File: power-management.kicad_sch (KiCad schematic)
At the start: 18 parts, among them Q3 DMP2070UQ-7, U2 AP2112K-3.3, U6 AP3602AKTR-G1

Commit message: Working on layout
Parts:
- Q3: footprint Package_TO_SOT_SMD:SOT-23-5_HandSoldering -> Package_TO_SOT_SMD:TSOT-23
- R38: footprint (none) -> Resistor_SMD:R_0805_2012Metric; Mfr (none) -> YAGEO; Mfr P/N (none) -> RC0805FR-07100KL; Supplier_1 (none) -> Digikey; Supplier_1 P/N (none) -> 311-100KCRCT-ND; Supplier_1 Price @ Qty (none) -> $0.00714; Supplier_1 Unit Price (none) -> $0.10000
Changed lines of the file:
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@@
 			)
 		)
-		(property "Footprint" "Package_TO_SOT_SMD:SOT-23-5_HandSoldering"
+		(property "Footprint" "Package_TO_SOT_SMD:TSOT-23"
 			(at 67.31 91.44 0)
 			(effects
@@
 					(size 1.27 1.27)
 				)
-				(hide yes)
 			)
 		)
@@
 			)
 		)
-		(property "Footprint" ""
+		(property "Footprint" "Resistor_SMD:R_0805_2012Metric"
 			(at 236.22 105.918 90)
 			(effects
@@
 			)
 		)
-		(property "Datasheet" "~"
+		(property "Datasheet" "https://www.yageo.com/upload/media/product/products/datasheet/rchip/PYu-RC_Group_51_RoHS_L_12.pdf"
 			(at 236.22 104.14 0)
 			(effects
@@
 			)
 		)
-		(property "Mfr" ""
-			(at 236.22 104.14 0)
-			(effects
-				(font
-					(size 1.27 1.27)
-				)
-				(hide yes)
-			)
-		)
-		(property "Mfr P/N" ""
-			(at 236.22 104.14 0)
-			(effects
-				(font
-					(size 1.27 1.27)
-				)
-				(hide yes)
-			)
-		)
-		(property "Supplier_1" ""
-			(at 236.22 104.14 0)
-			(effects
-				(font
-					(size 1.27 1.27)
-				)
-				(hide yes)
-			)
-		)
-		(property "Supplier_1 P/N" ""
-			(at 236.22 104.14 0)
-			(effects
-				(font
-					(size 1.27 1.27)
-				)
-				(hide yes)
-			)
-		)
-		(property "Supplier_1 Unit Price" ""
-			(at 236.22 104.14 0)
-			(effects
-				(font
-					(size 1.27 1.27)
-				)
-				(hide yes)
-			)
-		)
-		(property "Supplier_1 Price @ Qty" ""
-			(at 236.22 104.14 0)
-			(effects
+		(property "Mfr" "YAGEO"
+			(at 236.22 104.14 0)
+			(effects
+				(font
+					(size 1.27 1.27)
+				)
+				(hide yes)
+			)
+		)
+		(property "Mfr P/N" "RC0805FR-07100KL"
+			(at 236.22 104.14 0)
+			(effects
+				(font
+					(size 1.27 1.27)
+				)
+				(hide yes)
+			)
+		)
+		(property "Supplier_1" "Digikey"
+			(at 236.22 104.14 0)
+			(effects
+				(font
+					(size 1.27 1.27)
+				)
+				(hide yes)
+			)
+		)
+		(property "Supplier_1 P/N" "311-100KCRCT-ND"
+			(at 236.22 104.14 0)
+			(effects
+				(font
+					(size 1.27 1.27)
+				)
+				(hide yes)
+			)
+		)
+		(property "Supplier_1 Unit Price" "$0.10000 "
+			(at 236.22 104.14 0)
+			(effects
+				(font
+					(size 1.27 1.27)
+				)
+				(hide yes)
+			)
+		)
+		(property "Supplier_1 Price @ Qty" "$0.00714 "
+			(at 236.22 104.14 0)
+			(effects

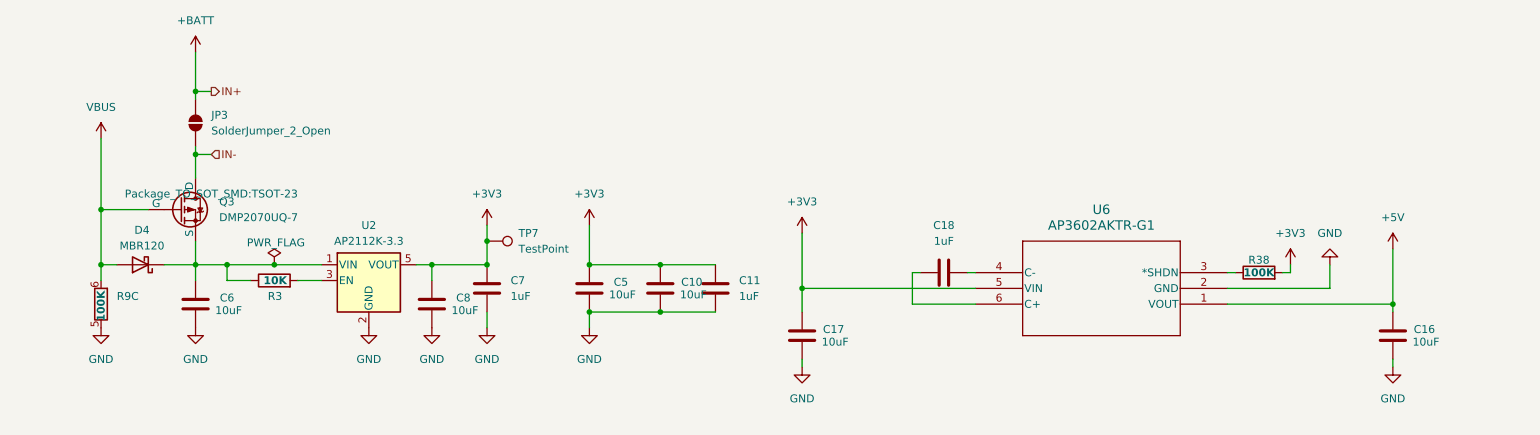
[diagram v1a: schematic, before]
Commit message: Redid board layout. Still have to add bypass caps
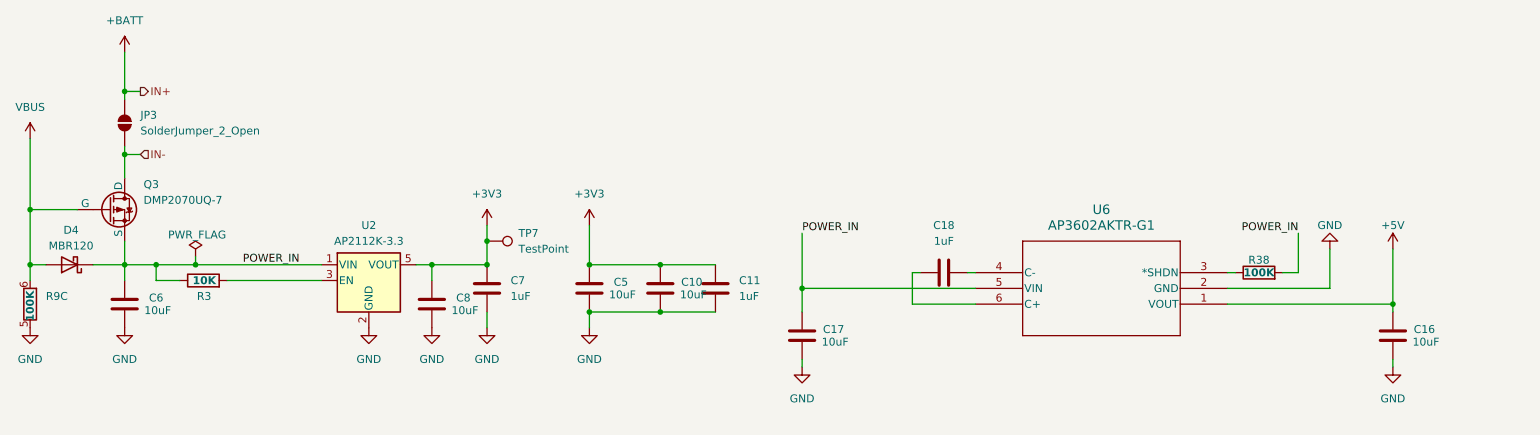
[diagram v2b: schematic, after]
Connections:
- net +3V3: no longer C17.1, R38.2, U6.5 (VIN)
- net POWER_IN: now reaches C6.1, D4.1 (K), Q3.3 (S), R3.1, U2.1 (VIN)
- net POWER_IN: now also C17.1, R38.2, U6.5 (VIN)
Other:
- moved on the sheet: C6, D4, JP3, Q3, R3, R9C

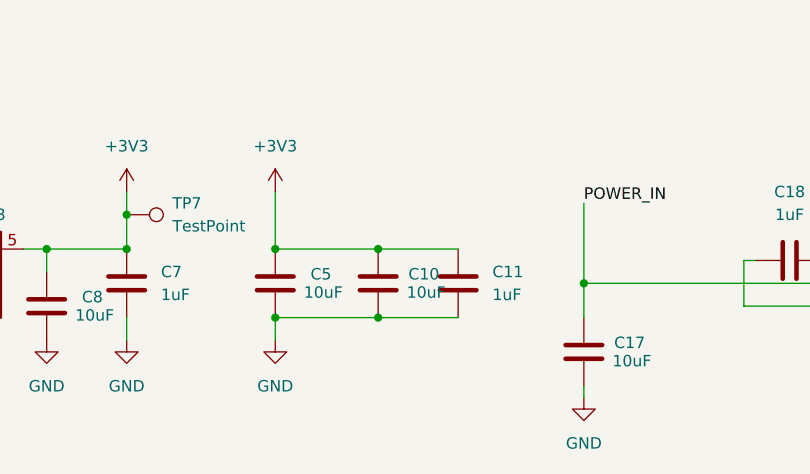
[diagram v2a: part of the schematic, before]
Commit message: Added mounting holes
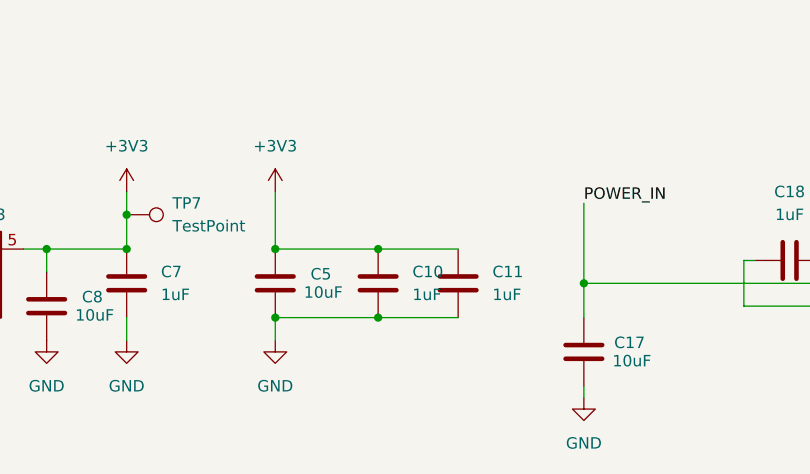
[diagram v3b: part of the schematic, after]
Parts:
- C10: value 10uF -> 1uF; footprint Inductor_SMD:L_0805_2012Metric -> Capacitor_SMD:C_0603_1608Metric; Mfr Samsung Electro-Mechanics -> YAGEO; Mfr P/N CL21A106KOQNNNE -> CC0603KRX7R7BB105; Supplier_1 P/N 1276-1096-1-ND -> 0.10; Supplier_1 Price @ Qty 0.03130 -> (none); Supplier_1 Unit Price 0.10 -> 0.03080
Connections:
- net +3V3: now also C10.2; no longer C10.1
- net GND: now also C10.1; no longer C10.2
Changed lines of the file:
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@@
 	)
 	(junction
-		(at 53.34 74.93)
+		(at 139.7 102.87)
 		(diameter 0)
 		(color 0 0 0 0)
 	)
 	(junction
-		(at 102.87 102.87)
+		(at 53.34 74.93)
 		(diameter 0)
 		(color 0 0 0 0)
 	)
 	(junction
-		(at 139.7 102.87)
+		(at 102.87 102.87)
 		(diameter 0)
 		(color 0 0 0 0)
@@
 	)
 	(junction
-		(at 111.76 102.87)
+		(at 139.7 110.49)
 		(diameter 0)
 		(color 0 0 0 0)
 	)
 	(junction
-		(at 139.7 110.49)
+		(at 111.76 102.87)
 		(diameter 0)
 		(color 0 0 0 0)
@@
 	(wire
 		(pts
+			(xy 139.7 102.87) (xy 148.59 102.87)
+		)
+		(stroke
+			(width 0)
+			(type default)
+		)
+	)
+	(wire
+		(pts
 			(xy 48.26 102.87) (xy 53.34 102.87)
 		)
@@
 	(wire
 		(pts
-			(xy 242.57 97.79) (xy 242.57 104.14)
+			(xy 139.7 110.49) (xy 148.59 110.49)
 		)
 		(stroke
@@
 	(wire
 		(pts
-			(xy 38.1 93.98) (xy 38.1 102.87)
+			(xy 242.57 97.79) (xy 242.57 104.14)
 		)
 		(stroke
@@
 	(wire
 		(pts
-			(xy 64.77 102.87) (xy 85.09 102.87)
+			(xy 38.1 93.98) (xy 38.1 102.87)
 		)
 		(stroke
@@
 	(wire
 		(pts
-			(xy 55.88 74.93) (xy 53.34 74.93)
+			(xy 64.77 102.87) (xy 85.09 102.87)
 		)
 		(stroke
@@
 	(wire
 		(pts
-			(xy 128.27 96.52) (xy 128.27 102.87)
+			(xy 55.88 74.93) (xy 53.34 74.93)
 		)
 		(stroke
@@
 	(wire
 		(pts
-			(xy 128.27 110.49) (xy 128.27 113.03)
+			(xy 128.27 96.52) (xy 128.27 102.87)
 		)
 		(stroke
@@
 	(wire
 		(pts
-			(xy 111.76 99.06) (xy 111.76 102.87)
+			(xy 128.27 110.49) (xy 128.27 113.03)
 		)
 		(stroke
@@
 	(wire
 		(pts
-			(xy 232.41 104.14) (xy 231.14 104.14)
+			(xy 111.76 99.06) (xy 111.76 102.87)
 		)
 		(stroke
@@
 	(wire
 		(pts
-			(xy 128.27 102.87) (xy 139.7 102.87)
+			(xy 232.41 104.14) (xy 231.14 104.14)
 		)
 		(stroke
@@
 	(wire
 		(pts
-			(xy 139.7 102.87) (xy 148.59 102.87)
+			(xy 128.27 102.87) (xy 139.7 102.87)
 		)
 		(stroke
@@
 	(wire
 		(pts
-			(xy 139.7 110.49) (xy 148.59 110.49)
-		)
-		(stroke
-			(width 0)
-			(type default)
-		)
-	)
-	(wire
-		(pts
 			(xy 128.27 110.49) (xy 139.7 110.49)
 		)
@@
 	)
 	(symbol
+		(lib_id "Device:C")
+		(at 139.7 106.68 180)
+		(unit 1)
+		(exclude_from_sim no)
+		(in_bom yes)
+		(on_board yes)
+		(dnp no)
+		(fields_autoplaced yes)
+		(property "Reference" "C10"
+			(at 143.51 105.4099 0)
+			(effects
+				(font
+					(size 1.27 1.27)
+				)
+				(justify right)
+			)
+		)
+		(property "Value" "1uF"
+			(at 143.51 107.9499 0)
+			(effects
+				(font
+					(size 1.27 1.27)
+				)
+				(justify right)
+			)
+		)
+		(property "Footprint" "Capacitor_SMD:C_0603_1608Metric"
+			(at 138.7348 102.87 0)
+			(effects
+				(font
+					(size 1.27 1.27)
+				)
+				(hide yes)
+			)
+		)
+		(property "Datasheet" "https://www.yageo.com/upload/media/product/productsearch/datasheet/mlcc/UPY-GPHC_X7R_6"
+			(at 139.7 106.68 0)
+			(effects
+				(font
+					(size 1.27 1.27)
+					(italic yes)
+				)
+				(hide yes)
+			)
+		)
+		(property "Description" "1 uF 10% 16V Ceramic Capacitor X7R 0603 (1608 Metric)"
+			(at 139.7 106.68 0)
+			(effects
+				(font
+					(size 1.27 1.27)
+				)
+				(hide yes)
+			)
+		)
+		(property "Mfr" "YAGEO"
+			(at 139.7 106.68 0)
+			(effects
+				(font
+					(size 1.27 1.27)
+				)
+				(hide yes)
+			)
+		)
+		(property "Mfr P/N" "CC0603KRX7R7BB105"
+			(at 139.7 106.68 0)
+			(effects
+				(font
+					(size 1.27 1.27)
+					(thickness 0.1588)
+				)
+				(hide yes)
+			)
+		)
+		(property "Supplier_1" "Digikey"
+			(at 139.7 106.68 0)
+			(effects
+				(font
+					(size 1.27 1.27)
+				)
+				(hide yes)
+			)
+		)
+		(property "Supplier_1 P/N" "0.10"
+			(at 139.7 106.68 0)
+			(effects
+				(font
+					(size 1.27 1.27)
+				)
+				(hide yes)
+			)
+		)
+		(property "Supplier_1 Unit Price" "0.03080"
+			(at 139.7 106.68 0)
+			(effects
+				(font
+					(size 1.27 1.27)
+				)
+				(hide yes)
+			)
+		)
+		(property "Supplier_1 Price @ Qty" ""
+			(at 139.7 106.68 0)
+			(effects
+				(font
+					(size 1.27 1.27)
+				)
+				(hide yes)
+			)
+		)
+		(property "Supplier_2" ""
+			(at 139.7 106.68 0)
+			(effects
+				(font
+					(size 1.27 1.27)
+				)
+				(hide yes)
+			)
+		)
+		(property "Supplier_2 P/N" ""
+			(at 139.7 106.68 0)
+			(effects
+				(font
+					(size 1.27 1.27)
+				)
+				(hide yes)
+			)
+		)
+		(property "Supplier_2 Unit Price" ""
+			(at 139.7 106.68 0)
+			(effects
+				(font
+					(size 1.27 1.27)
+				)
+				(hide yes)
+			)
+		)
+		(property "Supplier_2 Price @ Qty" ""
+			(at 139.7 106.68 0)
+			(effects
+				(font
+					(size 1.27 1.27)
+				)
+				(hide yes)
+			)
+		)
+		(pin "2"
+		)
+		(pin "1"
+		)
+		(instances
+			(project "roamer"
+				(path "/1c59de6a-87fe-4223-8898-4b0383164a31/f8947920-db82-4e9f-9d4f-25a180fcfca7"
+					(reference "C10")
+					(unit 1)
+				)
+			)
+		)
+	)
+	(symbol
 		(lib_id "power:GND")
 		(at 53.34 113.03 0)
@@
 					(unit 1)
 				)
-			)
-		)
-	)
-	(symbol
-		(lib_id "Device:C")
-		(at 139.7 106.68 0)
-		(unit 1)
-		(exclude_from_sim no)
-		(in_bom yes)
-		(on_board yes)
-		(dnp no)
-		(property "Reference" "C10"
-			(at 144.78 105.664 0)
-			(effects
-				(font
-					(size 1.27 1.27)
-				)
-			)
-		)
-		(property "Value" "10uF"
-			(at 145.034 107.696 0)
-			(effects
-				(font
-					(size 1.27 1.27)
-				)
-			)
-		)
-		(property "Footprint" "Inductor_SMD:L_0805_2012Metric"
-			(at 140.6652 110.49 0)
-			(effects
-				(font
-					(size 1.27 1.27)
-				)
-				(hide yes)
-			)
-		)
-		(property "Datasheet" "https://mm.digikey.com/Volume0/opasdata/d220001/medias/docus/609/CL21A106K0QNNNE_Sp"
-			(at 139.7 106.68 0)
-			(effects
-				(font
-					(size 1.27 1.27)
-				)
-				(hide yes)
-			)
-		)
-		(property "Description" "10 uF 10% 16V Ceramic Capacitor X5R 0805 (2012 Metric)"
-			(at 139.7 106.68 0)
-			(effects
-				(font
-					(size 1.27 1.27)
-				)
-				(hide yes)
-			)
-		)
-		(property "Mfr" "Samsung Electro-Mechanics"
-			(at 139.7 106.68 0)
-			(effects
-				(font
-					(size 1.27 1.27)
-				)
-				(hide yes)
-			)
-		)
-		(property "Mfr P/N" "CL21A106KOQNNNE"
-			(at 139.7 106.68 0)
-			(effects
-				(font
-					(size 1.27 1.27)
-				)
-				(hide yes)
-			)
-		)
-		(property "Supplier_1" "Digikey"
-			(at 139.7 106.68 0)
-			(effects
-				(font
-					(size 1.27 1.27)
-				)
-				(hide yes)
-			)
-		)
-		(property "Supplier_1 P/N" "1276-1096-1-ND"
-			(at 139.7 106.68 0)
-			(effects
-				(font
-					(size 1.27 1.27)
-				)
-				(hide yes)
-			)
-		)
-		(property "Supplier_1 Unit Price" "0.10"
-			(at 139.7 106.68 0)
-			(effects
-				(font
-					(size 1.27 1.27)
-				)
-				(hide yes)
-			)
-		)
-		(property "Supplier_1 Price @ Qty" "0.03130"
-			(at 139.7 106.68 0)
-			(effects
-				(font
-					(size 1.27 1.27)
-				)
-				(hide yes)
-			)
-		)
-		(property "Supplier_2" ""
-			(at 139.7 106.68 0)
-			(effects
-				(font
-					(size 1.27 1.27)
-				)
-				(hide yes)
-			)
-		)
-		(property "Supplier_2 P/N" ""
-			(at 139.7 106.68 0)
-			(effects
-				(font
-					(size 1.27 1.27)
-				)
-				(hide yes)
-			)
-		)
-		(property "Supplier_2 Unit Price" ""
-			(at 139.7 106.68 0)
-			(effects
-				(font
-					(size 1.27 1.27)
-				)
-				(hide yes)
-			)
-		)
-		(property "Supplier_2 Price @ Qty" ""
-			(at 139.7 106.68 0)
-			(effects
-				(font
-					(size 1.27 1.27)
-				)
-				(hide yes)
-			)
-		)
-		(pin "1"
-		)
-		(pin "2"
-		)
-		(instances
-			(project "roamer"
-				(path "/1c59de6a-87fe-4223-8898-4b0383164a31/f8947920-db82-4e9f-9d4f-25a180fcfca7"
-					(reference "C10")
-					(unit 1)
-				)

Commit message: Adding finishing touches
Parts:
- added TP1, TP2, TP5: TestPoint, TestPoint:TestPoint_Loop_D2.50mm_Drill1.0mm, symbol Connector:TestPoint
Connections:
- net +5V: now also TP5.1
- net +BATT: now also TP2.1
- net VBUS: now also TP1.1

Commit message: Creating fab package
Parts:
- added TP6: GND Testpoint, TestPoint:TestPoint_Loop_D2.50mm_Drill1.0mm, symbol Connector:TestPoint
- R38: Supplier_1 Price @ Qty $0.00714 -> 0.00714; Supplier_1 Unit Price $0.10000 -> 0.10000
- R9: value 100K -> 4x 100K
- TP1: value TestPoint -> VBUS Testpoint
- TP2: value TestPoint -> Batt Testpoint
- TP5: value TestPoint -> 5V Testpoint; Supplier_1 Price @ Qty $0.14964 -> 0.14964; Supplier_1 Unit Price $0.41000 -> 0.41000
- TP7: value TestPoint -> 3V3 Testpoint
- U6: Supplier_1 Unit Price $0.78000 -> 0.78000
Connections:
- net GND: now also TP6.1
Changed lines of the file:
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@@
 	)
 	(junction
+		(at 257.81 119.38)
+		(diameter 0)
+		(color 0 0 0 0)
+	)
+	(junction
 		(at 139.7 110.49)
 		(diameter 0)
@@
 	(wire
 		(pts
-			(xy 257.81 118.11) (xy 257.81 119.38)
+			(xy 55.88 85.09) (xy 53.34 85.09)
 		)
 		(stroke
@@
 	(wire
 		(pts
-			(xy 55.88 85.09) (xy 53.34 85.09)
+			(xy 38.1 85.09) (xy 38.1 93.98)
 		)
 		(stroke
@@
 	(wire
 		(pts
-			(xy 38.1 85.09) (xy 38.1 93.98)
+			(xy 111.76 110.49) (xy 111.76 113.03)
 		)
 		(stroke
@@
 	(wire
 		(pts
-			(xy 111.76 110.49) (xy 111.76 113.03)
+			(xy 231.14 109.22) (xy 257.81 109.22)
 		)
 		(stroke
@@
 	(wire
 		(pts
-			(xy 231.14 109.22) (xy 257.81 109.22)
+			(xy 257.81 119.38) (xy 257.81 118.11)
 		)
 		(stroke
@@
 	(wire
 		(pts
+			(xy 257.81 119.38) (xy 257.81 121.92)
+		)
+		(stroke
+			(width 0)
+			(type default)
+		)
+	)
+	(wire
+		(pts
 			(xy 53.34 102.87) (xy 53.34 105.41)
 		)
@@
 			)
 		)
-		(property "Value" "TestPoint"
+		(property "Value" "Batt Testpoint"
 			(at 58.42 71.1199 90)
 			(effects
@@
 			)
 		)
-		(property "Value" "TestPoint"
+		(property "Value" "5V Testpoint"
 			(at 262.89 104.1399 90)
 			(effects
@@
 			)
 		)
-		(property "Supplier_1 Unit Price" "$0.41000 "
+		(property "Supplier_1 Unit Price" "0.41000 "
 			(at 257.81 102.87 0)
 			(effects
@@
 			)
 		)
-		(property "Supplier_1 Price @ Qty" "$0.14964 "
+		(property "Supplier_1 Price @ Qty" "0.14964 "
 			(at 257.81 102.87 0)
 			(effects
@@
 			)
 		)
-		(property "Supplier_1 Unit Price" "$0.10000 "
+		(property "Supplier_1 Unit Price" "0.10000 "
 			(at 236.22 104.14 0)
 			(effects
@@
 			)
 		)
-		(property "Supplier_1 Price @ Qty" "$0.00714 "
+		(property "Supplier_1 Price @ Qty" "0.00714 "
 			(at 236.22 104.14 0)
 			(effects
@@
 			)
 		)
-		(property "Value" "TestPoint"
+		(property "Value" "3V3 Testpoint"
 			(at 116.84 100.3299 90)
 			(effects
@@
 			)
 		)
-		(property "Value" "100K"
+		(property "Value" "4x 100K"
 			(at 38.1 112.014 90)
 			(effects
@@
 			)
 		)
-		(property "Supplier_1 Unit Price" "$0.78000 "
+		(property "Supplier_1 Unit Price" "0.78000 "
 			(at 232.41 123.19 0)
 			(effects
@@
 	)
 	(symbol
+		(lib_id "Connector:TestPoint")
+		(at 257.81 119.38 270)
+		(unit 1)
+		(exclude_from_sim no)
+		(in_bom yes)
+		(on_board yes)
+		(dnp no)
+		(fields_autoplaced yes)
+		(property "Reference" "TP6"
+			(at 262.89 118.1099 90)
+			(effects
+				(font
+					(size 1.27 1.27)
+				)
+				(justify left)
+			)
+		)
+		(property "Value" "GND Testpoint"
+			(at 262.89 120.6499 90)
+			(effects
+				(font
+					(size 1.27 1.27)
+				)
+				(justify left)
+			)
+		)
+		(property "Footprint" "TestPoint:TestPoint_Loop_D2.50mm_Drill1.0mm"
+			(at 257.81 124.46 0)
+			(effects
+				(font
+					(size 1.27 1.27)
+				)
+				(hide yes)
+			)
+		)
+		(property "Datasheet" "https://www.keyelco.com/userAssets/file/M65p56.pdf"
+			(at 257.81 124.46 0)
+			(effects
+				(font
+					(size 1.27 1.27)
+				)
+				(hide yes)
+			)
+		)
+		(property "Description" "test point"
+			(at 257.81 119.38 0)
+			(effects
+				(font
+					(size 1.27 1.27)
+				)
+				(hide yes)
+			)
+		)
+		(property "Mfr" "Keystone Electronics"
+			(at 257.81 119.38 0)
+			(effects
+				(font
+					(size 1.27 1.27)
+				)
+				(hide yes)
+			)
+		)
+		(property "Mfr P/N" "5001"
+			(at 257.81 119.38 0)
+			(effects
+				(font
+					(size 1.27 1.27)
+				)
+				(hide yes)
+			)
+		)
+		(property "Supplier_1" "Digikey"
+			(at 257.81 119.38 0)
+			(effects
+				(font
+					(size 1.27 1.27)
+				)
+				(hide yes)
+			)
+		)
+		(property "Supplier_1 P/N" "36-5001-ND"
+			(at 257.81 119.38 0)
+			(effects
+				(font
+					(size 1.27 1.27)
+				)
+				(hide yes)
+			)
+		)
+		(property "Supplier_1 Unit Price" "0.41000 "
+			(at 257.81 119.38 0)
+			(effects
+				(font
+					(size 1.27 1.27)
+				)
+				(hide yes)
+			)
+		)
+		(property "Supplier_1 Price @ Qty" "0.14964 "
+			(at 257.81 119.38 0)
+			(effects
+				(font
+					(size 1.27 1.27)
+				)
+				(hide yes)
+			)
+		)
+		(property "Supplier_2" ""
+			(at 257.81 119.38 0)
+			(effects
+				(font
+					(size 1.27 1.27)
+				)
+				(hide yes)
+			)
+		)
+		(property "Supplier_2 P/N" ""
+			(at 257.81 119.38 0)
+			(effects
+				(font
+					(size 1.27 1.27)
+				)
+				(hide yes)
+			)
+		)
+		(property "Supplier_2 Unit Price" ""
+			(at 257.81 119.38 0)
+			(effects
+				(font
+					(size 1.27 1.27)
+				)
+				(hide yes)
+			)
+		)
+		(property "Supplier_2 Price @ Qty" ""
+			(at 257.81 119.38 0)
+			(effects
+				(font
+					(size 1.27 1.27)
+				)
+				(hide yes)
+			)
+		)
+		(pin "1"
+		)
+		(instances
+			(project "roamer"
+				(path "/1c59de6a-87fe-4223-8898-4b0383164a31/f8947920-db82-4e9f-9d4f-25a180fcfca7"
+					(reference "TP6")
+					(unit 1)
+				)
+			)
+		)
+	)
+	(symbol
 		(lib_id "Device:C")
 		(at 257.81 114.3 0)
@@
 	(symbol
 		(lib_id "power:GND")
-		(at 257.81 119.38 0)
+		(at 257.81 121.92 0)
 		(unit 1)
 		(exclude_from_sim no)
@@
 		(fields_autoplaced yes)
 		(property "Reference" "#PWR056"
-			(at 257.81 125.73 0)
+			(at 257.81 128.27 0)
 			(effects
 				(font
@@
 		)
 		(property "Value" "GND"
-			(at 257.81 124.46 0)
+			(at 257.81 127 0)
 			(effects
 				(font
@@
 		)
 		(property "Footprint" ""
-			(at 257.81 119.38 0)
+			(at 257.81 121.92 0)
 			(effects
 				(font
@@
 		)
 		(property "Datasheet" ""
-			(at 257.81 119.38 0)
+			(at 257.81 121.92 0)
 			(effects
 				(font
@@
 		)
 		(property "Description" "Power symbol creates a global label with name \"GND\" , ground"
-			(at 257.81 119.38 0)
+			(at 257.81 121.92 0)
 			(effects
 				(font
@@
 			)
 		)
-		(property "Value" "TestPoint"
+		(property "Value" "VBUS Testpoint"
 			(at 43.18 86.3599 90)
 			(effects
